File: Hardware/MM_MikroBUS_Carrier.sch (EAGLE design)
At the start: 53 parts, among them J15 MICROMOD-2222-C, J2 QWIIC_RIGHT_ANGLE, J5 Vertical Qwiic Connector, J7 MIKROBUS_SMD_BLACK1, J9 CORTEX_JTAG_DEBUG_MINIMUM_PTH, U1 MCP73831, U2 AP7361C-33FGEUDFN-8

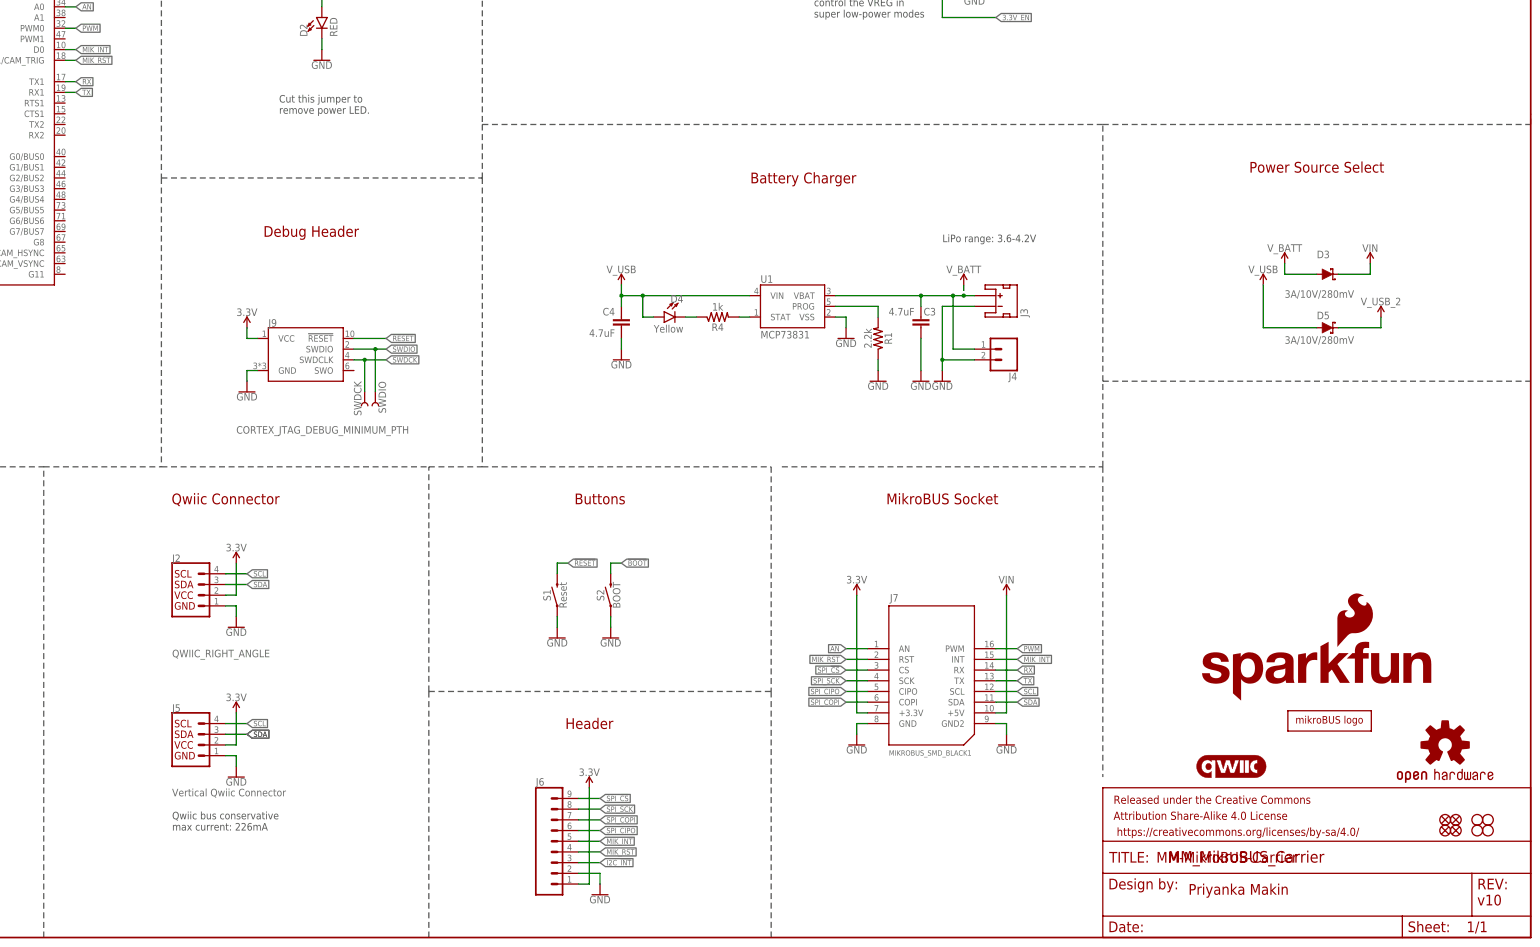
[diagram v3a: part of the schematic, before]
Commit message: v11 - switch RX and TX to match mikroBUS standard.
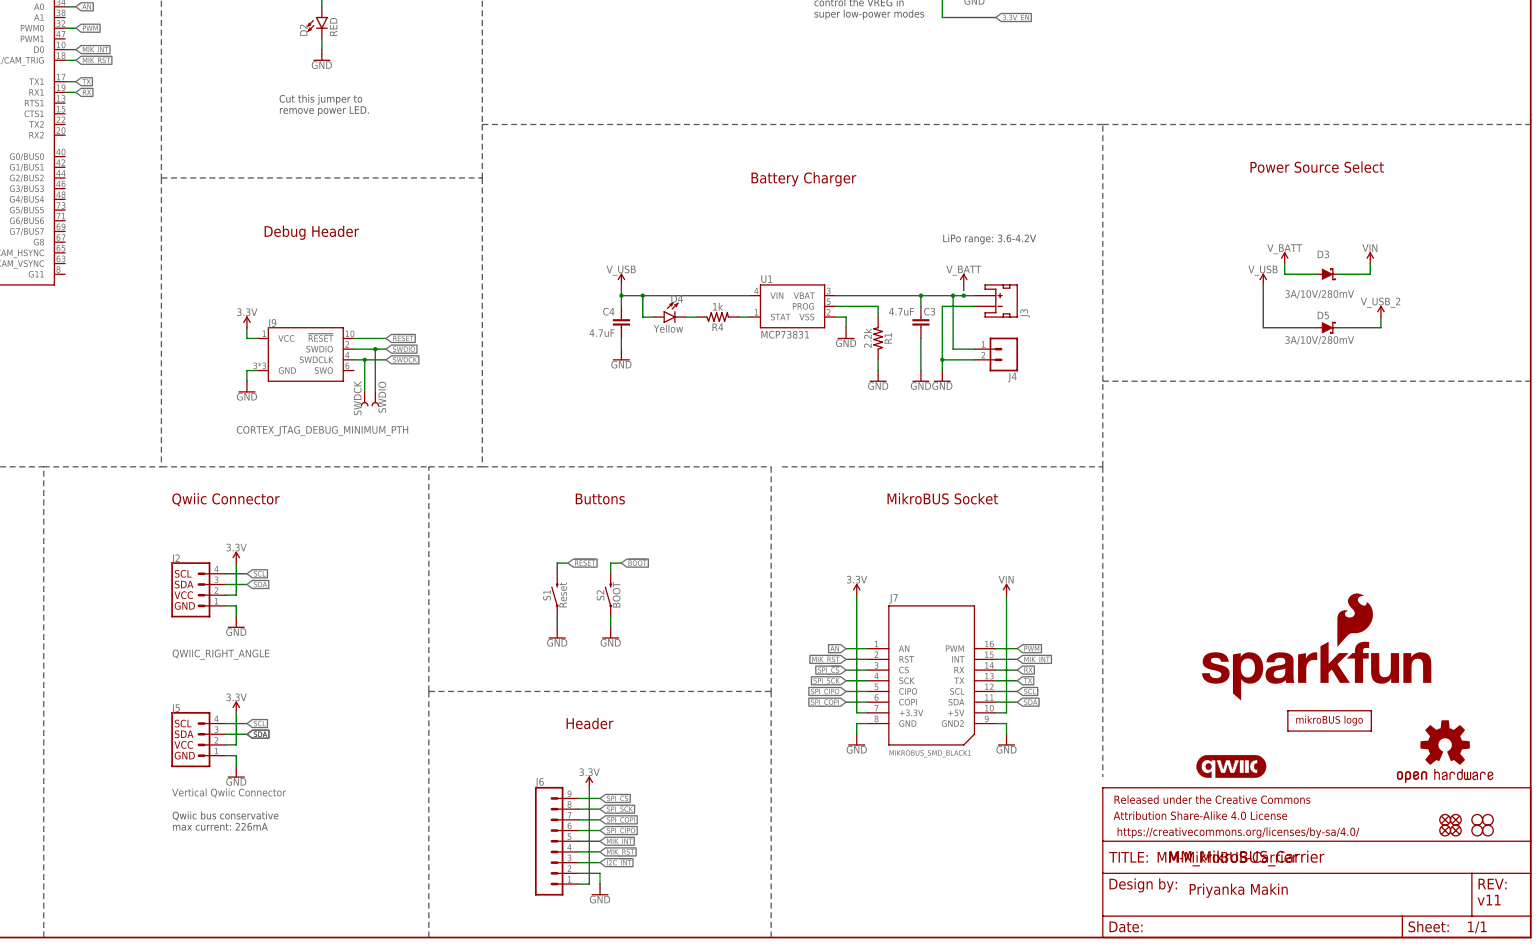
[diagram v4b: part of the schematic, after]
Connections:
- net RX: now also J15.RX1; no longer J15.TX1
- net TX: now also J15.TX1; no longer J15.RX1
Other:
- note added: "v11"
- note removed: "v10"
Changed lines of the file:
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@@
 <grid distance="0.1" unitdist="inch" unit="inch" style="lines" multiple="1" display="no" altdistance="0.01" altunitdist="inch" altunit="inch"/>
 <layers>
-<layer number="1" name="Top" color="4" fill="1" visible="yes" active="no"/>
-<layer number="2" name="Route2" color="1" fill="3" visible="yes" active="no"/>
-<layer number="3" name="Route3" color="4" fill="3" visible="yes" active="no"/>
-<layer number="4" name="Route4" color="1" fill="4" visible="yes" active="no"/>
-<layer number="5" name="Route5" color="4" fill="4" visible="yes" active="no"/>
-<layer number="6" name="Route6" color="1" fill="8" visible="yes" active="no"/>
-<layer number="7" name="Route7" color="4" fill="8" visible="yes" active="no"/>
-<layer number="8" name="Route8" color="1" fill="2" visible="yes" active="no"/>
-<layer number="9" name="Route9" color="4" fill="2" visible="yes" active="no"/>
-<layer number="10" name="Route10" color="1" fill="7" visible="yes" active="no"/>
-<layer number="11" name="Route11" color="4" fill="7" visible="yes" active="no"/>
-<layer number="12" name="Route12" color="1" fill="5" visible="yes" active="no"/>
-<layer number="13" name="Route13" color="4" fill="5" visible="yes" active="no"/>
-<layer number="14" name="Route14" color="1" fill="6" visible="yes" active="no"/>
-<layer number="15" name="Route15" color="4" fill="6" visible="yes" active="no"/>
-<layer number="16" name="Bottom" color="1" fill="1" visible="yes" active="no"/>
-<layer number="17" name="Pads" color="2" fill="1" visible="yes" active="no"/>
-<layer number="18" name="Vias" color="2" fill="1" visible="yes" active="no"/>
-<layer number="19" name="Unrouted" color="6" fill="1" visible="yes" active="no"/>
-<layer number="20" name="Dimension" color="24" fill="1" visible="yes" active="no"/>
-<layer number="21" name="tPlace" color="16" fill="1" visible="yes" active="no"/>
-<layer number="22" name="bPlace" color="14" fill="1" visible="yes" active="no"/>
-<layer number="23" name="tOrigins" color="15" fill="1" visible="yes" active="no"/>
-<layer number="24" name="bOrigins" color="15" fill="1" visible="yes" active="no"/>
-<layer number="25" name="tNames" color="7" fill="1" visible="yes" active="no"/>
-<layer number="26" name="bNames" color="7" fill="1" visible="yes" active="no"/>
-<layer number="27" name="tValues" color="7" fill="1" visible="yes" active="no"/>
-<layer number="28" name="bValues" color="7" fill="1" visible="yes" active="no"/>
+<layer number="1" name="Top" color="4" fill="1" visible="no" active="no"/>
+<layer number="2" name="Route2" color="1" fill="3" visible="no" active="no"/>
+<layer number="3" name="Route3" color="4" fill="3" visible="no" active="no"/>
+<layer number="4" name="Route4" color="1" fill="4" visible="no" active="no"/>
+<layer number="5" name="Route5" color="4" fill="4" visible="no" active="no"/>
+<layer number="6" name="Route6" color="1" fill="8" visible="no" active="no"/>
+<layer number="7" name="Route7" color="4" fill="8" visible="no" active="no"/>
+<layer number="8" name="Route8" color="1" fill="2" visible="no" active="no"/>
+<layer number="9" name="Route9" color="4" fill="2" visible="no" active="no"/>
+<layer number="10" name="Route10" color="1" fill="7" visible="no" active="no"/>
+<layer number="11" name="Route11" color="4" fill="7" visible="no" active="no"/>
+<layer number="12" name="Route12" color="1" fill="5" visible="no" active="no"/>
+<layer number="13" name="Route13" color="4" fill="5" visible="no" active="no"/>
+<layer number="14" name="Route14" color="1" fill="6" visible="no" active="no"/>
+<layer number="15" name="Route15" color="4" fill="6" visible="no" active="no"/>
+<layer number="16" name="Bottom" color="1" fill="1" visible="no" active="no"/>
+<layer number="17" name="Pads" color="2" fill="1" visible="no" active="no"/>
+<layer number="18" name="Vias" color="2" fill="1" visible="no" active="no"/>
+<layer number="19" name="Unrouted" color="6" fill="1" visible="no" active="no"/>
+<layer number="20" name="Dimension" color="24" fill="1" visible="no" active="no"/>
+<layer number="21" name="tPlace" color="16" fill="1" visible="no" active="no"/>
+<layer number="22" name="bPlace" color="14" fill="1" visible="no" active="no"/>
+<layer number="23" name="tOrigins" color="15" fill="1" visible="no" active="no"/>
+<layer number="24" name="bOrigins" color="15" fill="1" visible="no" active="no"/>
+<layer number="25" name="tNames" color="7" fill="1" visible="no" active="no"/>
+<layer number="26" name="bNames" color="7" fill="1" visible="no" active="no"/>
+<layer number="27" name="tValues" color="7" fill="1" visible="no" active="no"/>
+<layer number="28" name="bValues" color="7" fill="1" visible="no" active="no"/>
 <layer number="29" name="tStop" color="7" fill="3" visible="no" active="no"/>
 <layer number="30" name="bStop" color="7" fill="6" visible="no" active="no"/>
@@
 <layer number="35" name="tGlue" color="7" fill="4" visible="no" active="no"/>
 <layer number="36" name="bGlue" color="7" fill="5" visible="no" active="no"/>
-<layer number="37" name="tTest" color="7" fill="1" visible="yes" active="no"/>
-<layer number="38" name="bTest" color="7" fill="1" visible="yes" active="no"/>
+<layer number="37" name="tTest" color="7" fill="1" visible="no" active="no"/>
+<layer number="38" name="bTest" color="7" fill="1" visible="no" active="no"/>
 <layer number="39" name="tKeepout" color="4" fill="11" visible="no" active="no"/>
 <layer number="40" name="bKeepout" color="1" fill="11" visible="no" active="no"/>
@@
 <layer number="44" name="Drills" color="7" fill="1" visible="no" active="no"/>
 <layer number="45" name="Holes" color="7" fill="1" visible="no" active="no"/>
-<layer number="46" name="Milling" color="3" fill="1" visible="yes" active="no"/>
-<layer number="47" name="Measures" color="7" fill="1" visible="yes" active="no"/>
-<layer number="48" name="Document" color="7" fill="1" visible="yes" active="no"/>
-<layer number="49" name="Reference" color="7" fill="1" visible="yes" active="no"/>
-<layer number="50" name="dxf" color="7" fill="1" visible="yes" active="no"/>
-<layer number="51" name="tDocu" color="6" fill="1" visible="yes" active="no"/>
-<layer number="52" name="bDocu" color="7" fill="1" visible="yes" active="no"/>
-<layer number="53" name="tGND_GNDA" color="7" fill="9" visible="yes" active="no"/>
-<layer number="54" name="bGND_GNDA" color="1" fill="9" visible="yes" active="no"/>
-<layer number="56" name="wert" color="7" fill="1" visible="yes" active="no"/>
-<layer number="57" name="tCAD" color="7" fill="1" visible="yes" active="no"/>
-<layer number="58" name="bCAD" color="7" fill="1" visible="yes" active="no"/>
-<layer number="59" name="tCarbon" color="7" fill="1" visible="yes" active="no"/>
-<layer number="60" name="bCarbon" color="7" fill="1" visible="yes" active="no"/>
+<layer number="46" name="Milling" color="3" fill="1" visible="no" active="no"/>
+<layer number="47" name="Measures" color="7" fill="1" visible="no" active="no"/>
+<layer number="48" name="Document" color="7" fill="1" visible="no" active="no"/>
+<layer number="49" name="Reference" color="7" fill="1" visible="no" active="no"/>
+<layer number="50" name="dxf" color="7" fill="1" visible="no" active="no"/>
+<layer number="51" name="tDocu" color="6" fill="1" visible="no" active="no"/>
+<layer number="52" name="bDocu" color="7" fill="1" visible="no" active="no"/>
+<layer number="53" name="tGND_GNDA" color="7" fill="9" visible="no" active="no"/>
+<layer number="54" name="bGND_GNDA" color="1" fill="9" visible="no" active="no"/>
+<layer number="56" name="wert" color="7" fill="1" visible="no" active="no"/>
+<layer number="57" name="tCAD" color="7" fill="1" visible="no" active="no"/>
+<layer number="58" name="bCAD" color="7" fill="1" visible="no" active="no"/>
+<layer number="59" name="tCarbon" color="7" fill="1" visible="no" active="no"/>
+<layer number="60" name="bCarbon" color="7" fill="1" visible="no" active="no"/>
 <layer number="88" name="SimResults" color="9" fill="1" visible="yes" active="yes"/>
 <layer number="89" name="SimProbes" color="9" fill="1" visible="yes" active="yes"/>
@@
 <text x="342.9" y="17.78" size="2.54" layer="94" font="vector">MM-MikroBUS-Carrier</text>
 <text x="144.78" y="266.7" size="2.54" layer="94" font="vector" align="center">LED</text>
-<text x="419.1" y="7.62" size="2.54" layer="94" font="vector">v10</text>
+<text x="419.1" y="7.62" size="2.54" layer="94" font="vector">v11</text>
 <text x="134.62" y="195.58" size="1.778" layer="97" font="vector">Cut this jumper to
 remove power LED.</text>
@@
 </segment>
 <segment>
+<pinref part="J15" gate="J1" pin="RX1"/>
+<wire x1="83.82" y1="200.66" x2="86.36" y2="200.66" width="0.1524" layer="91"/>
+<label x="86.36" y="200.66" size="1.27" layer="95" xref="yes"/>
+</segment>
+</net>
+<net name="TX" class="0">
+<segment>
+<pinref part="J7" gate="J1" pin="TX"/>
+<wire x1="304.8" y1="60.96" x2="309.88" y2="60.96" width="0.1524" layer="91"/>
+<label x="309.88" y="60.96" size="1.27" layer="95" xref="yes"/>
+</segment>
+<segment>
 <pinref part="J15" gate="J1" pin="TX1"/>
 <wire x1="83.82" y1="203.2" x2="86.36" y2="203.2" width="0.1524" layer="91"/>
@@
 </segment>
 </net>
-<net name="TX" class="0">
-<segment>
-<pinref part="J7" gate="J1" pin="TX"/>
-<wire x1="304.8" y1="60.96" x2="309.88" y2="60.96" width="0.1524" layer="91"/>
-<label x="309.88" y="60.96" size="1.27" layer="95" xref="yes"/>
-</segment>
-<segment>
-<pinref part="J15" gate="J1" pin="RX1"/>
-<wire x1="83.82" y1="200.66" x2="86.36" y2="200.66" width="0.1524" layer="91"/>
-<label x="86.36" y="200.66" size="1.27" layer="95" xref="yes"/>
-</segment>
-</net>
